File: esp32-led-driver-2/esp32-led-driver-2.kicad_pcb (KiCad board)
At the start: 2 copper layers, 40 x 90 mm, 7 parts, among them J2 Conn_01x03_Female, J3 Conn_01x03_Female, J4 Conn_01x03_Female, J5 Conn_01x03_Female, U2 SN74AHCT125N

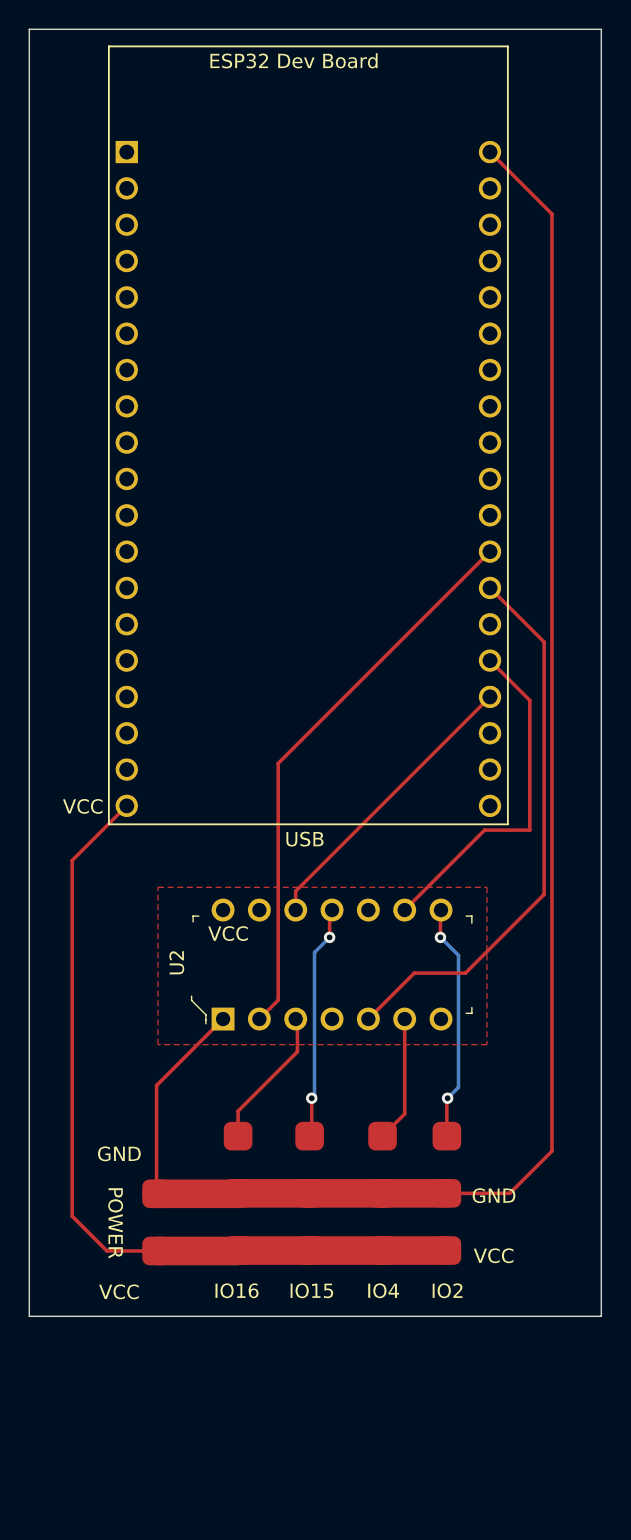
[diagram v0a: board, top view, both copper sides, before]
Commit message: Added macropad
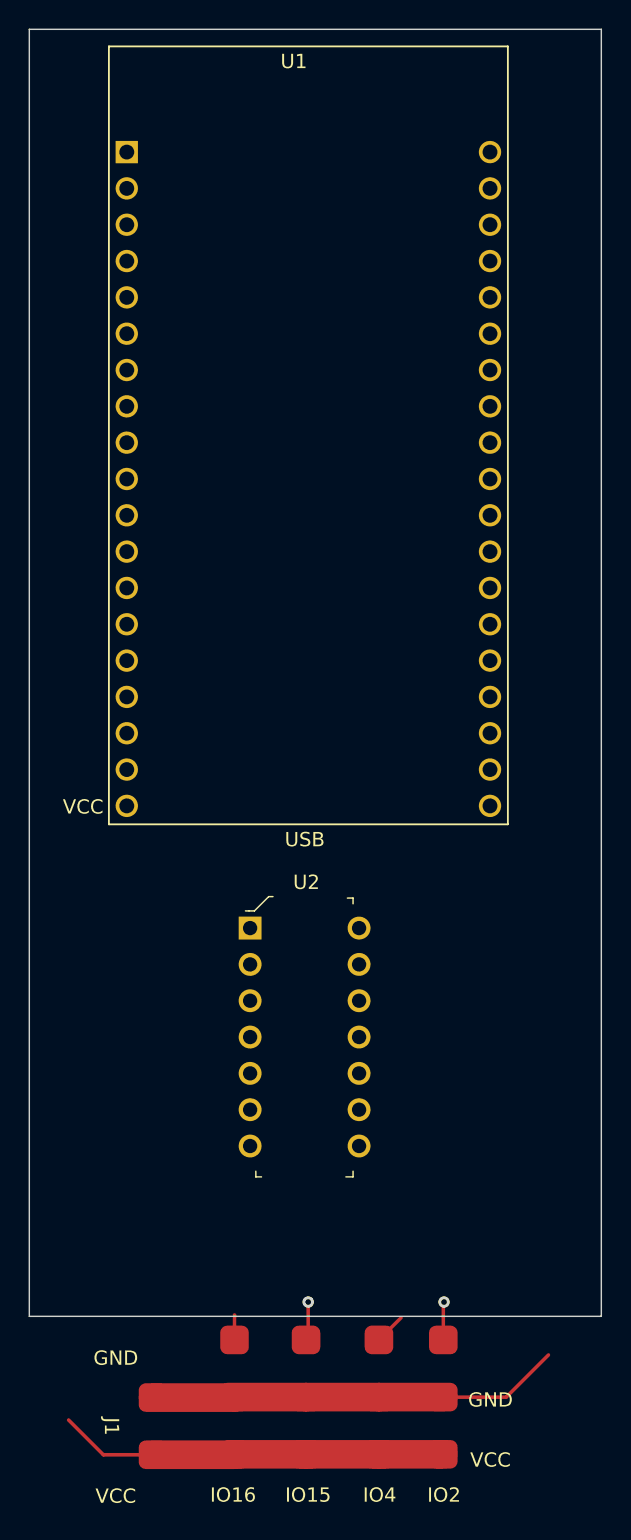
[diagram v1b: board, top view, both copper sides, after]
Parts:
- U1: renamed from ESP32 Dev Board
- moved J1 14.3 mm to (53.6, 162.8)
- moved J2 14.3 mm to (64.3, 160.7)
- moved J3 14.3 mm to (74.0, 160.7)
- moved J4 14.3 mm to (69.5, 160.7)
- moved J5 14.3 mm to (59.4, 160.7)
- moved U2 6.63 mm to (60.4, 127.8), turned to 0 degrees
- renumbered POWER to J1
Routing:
- net GND: track 114.7 -> 28.9 mm
- net /IO16: track 39.4 -> 0.00 mm
- net /IO4: track 38.9 -> 0.00 mm
- net VCC: track 57.5 -> 27.2 mm
- net /IO2: track 24.1 -> 0.00 mm
- net /IO15: track 20.5 -> 0.00 mm
- net /IO2_5v5: track 16.7 -> 2.67 mm, vias 2 -> 1
- net /IO15_5v5: track 16.5 -> 2.99 mm, vias 2 -> 1
- net /IO16_5v5: track 9.96 -> 1.75 mm
- net /IO4_5v5: track 8.83 -> 2.19 mm
- removed copper zone on F.Cu, net GND
